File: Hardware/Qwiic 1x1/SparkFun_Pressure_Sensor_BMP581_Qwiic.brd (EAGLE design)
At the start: 25.4 x 25.4 mm, 48 parts, among them J1 QWIIC_RIGHT_ANGLE, J2 QWIIC_RIGHT_ANGLE, U1 BMP581

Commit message: Add optional pullup on CSB
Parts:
- added JP4: LED, SparkFun-Jumpers:SMT-JUMPER_2_NC_TRACE_SILK
- added R6: 10k, SparkFun-Resistors:0603
- added U$18: (no value), output:##CSB##1
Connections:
- new net N$7: JP4.2, R6.1
- net !CSB!: now also JP4.1
- net VDD: now also R6.2
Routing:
- net VDD: track 46.1 -> 50.3 mm
- net N$7: track 0.00 -> 2.16 mm, vias 0 -> 1
- net !CSB!: track 13.3 -> 14.4 mm, vias 0 -> 1
- net GND: vias 28 -> 30
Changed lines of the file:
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@@
 <drawing>
 <settings>
-<setting alwaysvectorfont="no"/>
+<setting alwaysvectorfont="yes"/>
 <setting verticaltext="up"/>
 </settings>
@@
 <element name="U$15" library="output" package="#0X47#0" value="" x="11.303" y="15.875" smashed="yes" rot="MR0"/>
 <element name="U$16" library="output" package="PWR0" value="" x="22.86" y="20.32" smashed="yes"/>
+<element name="JP4" library="SparkFun-Jumpers" package="SMT-JUMPER_2_NC_TRACE_SILK" package3d_urn="urn:adsk.eagle:package:39281/1" value="LED" x="19.05" y="7.112" smashed="yes" rot="MR180">
+<attribute name="NAME" x="19.05" y="5.969" size="0.6096" layer="26" font="vector" ratio="20" rot="MR180" align="bottom-center"/>
+<attribute name="VALUE" x="19.05" y="8.255" size="0.6096" layer="28" font="vector" ratio="20" rot="MR180" align="top-center"/>
+</element>
+<element name="R6" library="SparkFun-Resistors" package="0603" value="10k" x="21.59" y="7.62" smashed="yes" rot="R90">
+<attribute name="NAME" x="20.828" y="7.62" size="0.6096" layer="25" font="vector" ratio="20" rot="R90" align="bottom-center"/>
+<attribute name="PROD_ID" value="RES-00824" x="21.59" y="7.62" size="1.778" layer="27" rot="R90" display="off"/>
+<attribute name="VALUE" x="22.352" y="7.62" size="0.6096" layer="27" font="vector" ratio="20" rot="R90" align="top-center"/>
+</element>
+<element name="U$18" library="output" package="##CSB##1" value="" x="19.939" y="7.112" smashed="yes" rot="MR0"/>
 </elements>
 <signals>
@@
 <wire x1="11.307" y1="12.95" x2="11.9375" y2="12.95" width="0.254" layer="1"/>
 <wire x1="10.573684375" y1="13.683315625" x2="11.307" y2="12.95" width="0.254" layer="1"/>
+<contactref element="R6" pad="2"/>
+<wire x1="22.1869" y1="10.92875" x2="22.1869" y2="11.55025" width="0.1778" layer="1"/>
+<wire x1="21.59" y1="8.47" x2="21.59" y2="10.33185" width="0.1778" layer="1"/>
+<wire x1="21.59" y1="12.14715" x2="21.59" y2="12.192" width="0.1778" layer="1"/>
+<wire x1="21.59" y1="10.33185" x2="22.1869" y2="10.92875" width="0.1778" layer="1"/>
+<wire x1="22.1869" y1="11.55025" x2="21.59" y2="12.14715" width="0.1778" layer="1"/>
 </signal>
 <signal name="GND">
@@
 <wire x1="12.7" y1="13.4625" x2="12.7" y2="14.224" width="0.254" layer="1"/>
 <wire x1="13.2" y1="13.4625" x2="13.2" y2="14.224" width="0.254" layer="1"/>
+<via x="22.86" y="11.303" extent="1-16" drill="0.3048"/>
+<via x="19.05" y="5.715" extent="1-16" drill="0.3048"/>
 </signal>
 <signal name="SDI/SDA">
@@
 <contactref element="U1" pad="6"/>
 <contactref element="J3" pad="6"/>
-<wire x1="17.78" y1="1.27" x2="17.78" y2="8.763" width="0.254" layer="1"/>
+<wire x1="17.78" y1="1.27" x2="17.78" y2="6.985" width="0.254" layer="1"/>
+<wire x1="17.78" y1="6.985" x2="17.78" y2="8.763" width="0.254" layer="1"/>
 <wire x1="14.093" y1="12.45" x2="13.4625" y2="12.45" width="0.254" layer="1"/>
 <wire x1="17.78" y1="8.763" x2="14.093" y2="12.45" width="0.254" layer="1"/>
+<contactref element="JP4" pad="1"/>
+<wire x1="18.5293" y1="7.112" x2="18.4023" y2="6.985" width="0.1778" layer="16"/>
+<wire x1="18.4023" y1="6.985" x2="17.6304" y2="6.985" width="0.1778" layer="16"/>
+<via x="17.6304" y="6.985" extent="1-16" drill="0.35"/>
+<wire x1="17.6304" y1="6.985" x2="17.78" y2="6.985" width="0.1778" layer="1"/>
 </signal>
 <signal name="N$1">
@@
 <wire x1="23.456" y1="19.023" x2="23.483" y2="19.05" width="0.254" layer="1"/>
 </signal>
+<signal name="N$7">
+<contactref element="JP4" pad="2"/>
+<contactref element="R6" pad="1"/>
+<wire x1="19.5707" y1="7.112" x2="20.447" y2="7.112" width="0.1778" layer="16"/>
+<via x="20.447" y="7.112" extent="1-16" drill="0.35"/>
+<wire x1="20.447" y1="7.112" x2="20.789" y2="6.77" width="0.1778" layer="1"/>
+<wire x1="20.789" y1="6.77" x2="21.59" y2="6.77" width="0.1778" layer="1"/>
+</signal>
 </signals>

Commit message: Rename CSB pullup jumper in schematic
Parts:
- JP4: value LED -> !CSB!
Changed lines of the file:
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@@
 <drawing>
 <settings>
-<setting alwaysvectorfont="yes"/>
+<setting alwaysvectorfont="no"/>
 <setting verticaltext="up"/>
 </settings>
@@
 <element name="U$15" library="output" package="#0X47#0" value="" x="11.303" y="15.875" smashed="yes" rot="MR0"/>
 <element name="U$16" library="output" package="PWR0" value="" x="22.86" y="20.32" smashed="yes"/>
-<element name="JP4" library="SparkFun-Jumpers" package="SMT-JUMPER_2_NC_TRACE_SILK" package3d_urn="urn:adsk.eagle:package:39281/1" value="LED" x="19.05" y="7.112" smashed="yes" rot="MR180">
+<element name="JP4" library="SparkFun-Jumpers" package="SMT-JUMPER_2_NC_TRACE_SILK" package3d_urn="urn:adsk.eagle:package:39281/1" value="!CSB!" x="19.05" y="7.112" smashed="yes" rot="MR180">
 <attribute name="NAME" x="19.05" y="5.969" size="0.6096" layer="26" font="vector" ratio="20" rot="MR180" align="bottom-center"/>
 <attribute name="VALUE" x="19.05" y="8.255" size="0.6096" layer="28" font="vector" ratio="20" rot="MR180" align="top-center"/>

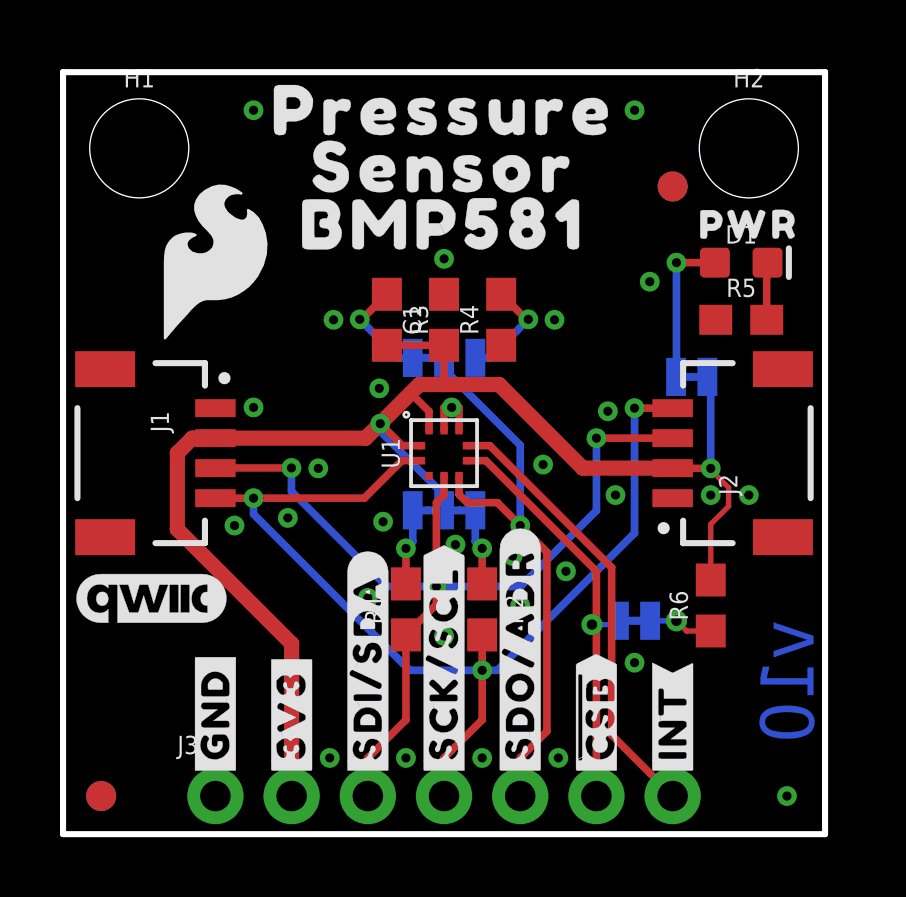
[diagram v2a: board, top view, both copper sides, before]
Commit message: Design review updates
Change INT label to fishtail in Micro silk
Add product name to bottom in 1x1 silk
Change Micro net labels to be I2C only
Approve DRC overlaps
Fix acid trap
Add note about CSB being tied high in Micro schematic
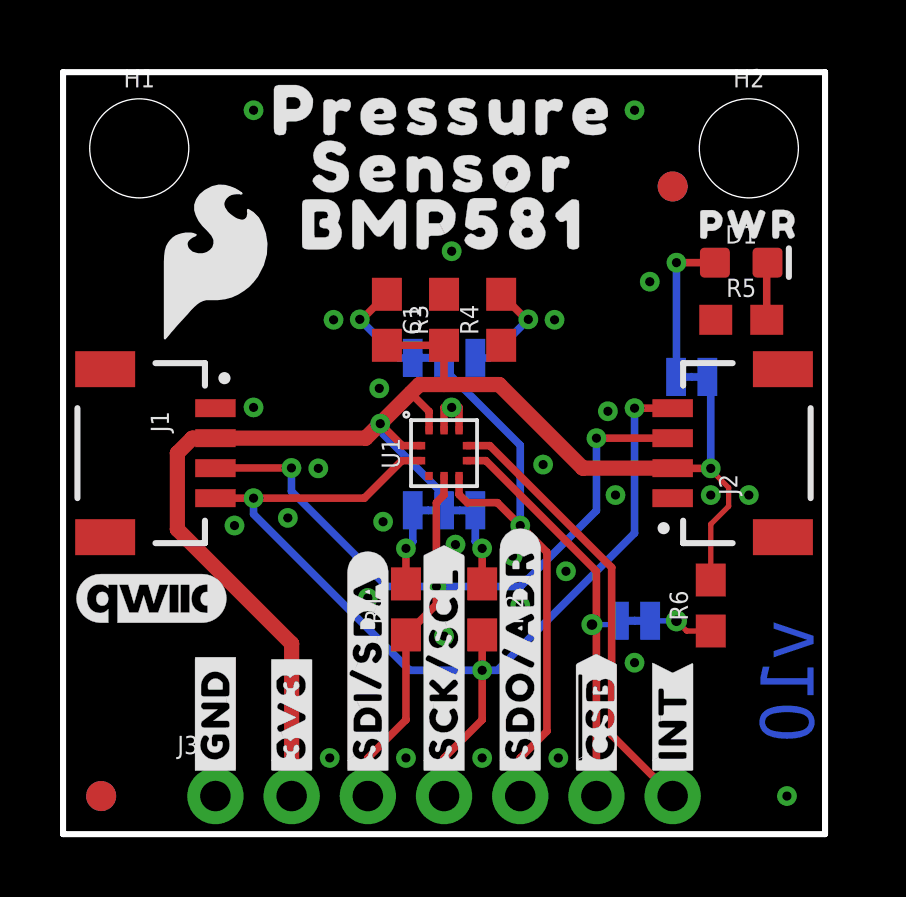
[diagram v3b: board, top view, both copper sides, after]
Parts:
- added U$22: (no value), output:BMP5810
- moved LOGO4 1.27 mm to (12.7, 21.6)
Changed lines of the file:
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@@
 <drawing>
 <settings>
-<setting alwaysvectorfont="no"/>
+<setting alwaysvectorfont="yes"/>
 <setting verticaltext="up"/>
 </settings>
@@
 <element name="LOGO2" library="SparkFun-Aesthetics" package="SFE_LOGO_FLAME_.2" value="SFE_LOGO_FLAME.2_INCH" x="5.08" y="19.05" smashed="yes"/>
 <element name="LOGO3" library="SparkFun-Aesthetics" package="QWIIC_5MM" value="QWIIC_LOGO_5MM" x="2.921" y="7.874" smashed="yes"/>
-<element name="LOGO4" library="SparkFun-Aesthetics" package="SFE_LOGO_NAME_FLAME_.1" value="SFE_LOGO_NAME_FLAME.1_INCH" x="12.7" y="20.32" smashed="yes" rot="MR0"/>
+<element name="LOGO4" library="SparkFun-Aesthetics" package="SFE_LOGO_NAME_FLAME_.1" value="SFE_LOGO_NAME_FLAME.1_INCH" x="12.7" y="21.59" smashed="yes" rot="MR0"/>
 <element name="R1" library="SparkFun-Resistors" package="0603" value="2.2k" x="11.43" y="7.493" smashed="yes" rot="R90">
 <attribute name="NAME" x="10.668" y="7.493" size="0.6096" layer="25" font="vector" ratio="20" rot="R90" align="bottom-center"/>
@@
 </element>
 <element name="U$18" library="output" package="##CSB##1" value="" x="19.939" y="7.112" smashed="yes" rot="MR0"/>
+<element name="U$22" library="output" package="BMP5810" value="" x="12.7" y="19.177" smashed="yes" rot="MR0"/>
 </elements>
 <signals>
@@
 <via x="19.05" y="24.13" extent="1-16" drill="0.3048"/>
 <via x="6.35" y="24.13" extent="1-16" drill="0.3048"/>
-<via x="12.7" y="19.177" extent="1-16" drill="0.3048"/>
+<via x="12.954" y="19.431" extent="1-16" drill="0.3048"/>
 <via x="10.668" y="10.414" extent="1-16" drill="0.3048"/>
 <via x="8.89" y="2.54" extent="1-16" drill="0.3048"/>

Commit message: Remove library file
BMP384 is in SFE Eagle library, update part in design
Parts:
- U1: device BMP581:BMP581 -> SparkFun-Sensors:BMP581
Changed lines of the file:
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@@
 <attribute name="VALUE" x="22.606" y="16.383" size="0.6096" layer="27" font="vector" ratio="20" align="top-center"/>
 </element>
-<element name="U1" library="BMP581" package="BMP581" value="BMP581" x="12.7" y="12.7" smashed="yes" rot="R90">
+<element name="U1" library="SparkFun-Sensors" package="BMP581" value="BMP581" x="12.7" y="12.7" smashed="yes" rot="R90">
 <attribute name="NAME" x="10.922" y="12.7" size="0.6096" layer="25" font="vector" ratio="20" rot="R90" align="center"/>
 <attribute name="PROD_ID" value="IC-16798" x="31.75" y="43.18" size="1.778" layer="27" rot="R90" display="off"/>
